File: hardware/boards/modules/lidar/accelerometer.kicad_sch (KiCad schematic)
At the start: 7 parts, among them J8 Conn_01x04_Socket, U2 BNO055, Y2 32.768kHz

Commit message: REFACTO relinked every kicad projects
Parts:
- U2: footprint accelerometer:BNO055_Hand_Soldering_LGA-28_5.2x3.8mm_P0.5mm -> Package_LGA:LGA-28_5.2x3.8mm_P0.5mm
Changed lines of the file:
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@@
 			)
 		)
-		(property "Footprint" "accelerometer:BNO055_Hand_Soldering_LGA-28_5.2x3.8mm_P0.5mm"
+		(property "Footprint" "Package_LGA:LGA-28_5.2x3.8mm_P0.5mm"
 			(at 148.59 133.35 0)
 			(effects

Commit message: updated main points of the lidar module schematic
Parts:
- C7, C8: value 0.1uF -> 100nF
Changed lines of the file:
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@@
 			)
 		)
-		(property "Value" "0.1uF"
+		(property "Value" "100nF"
 			(at 137.414 93.726 90)
 			(effects
@@
 			)
 		)
-		(property "Value" "0.1uF"
+		(property "Value" "100nF"
 			(at 163.068 137.414 0)
 			(effects

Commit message: lidar PCB
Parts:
- removed J8: Conn_01x04_Socket, Connector_PinHeader_2.54mm:PinHeader_1x04_P2.54mm_Vertical, symbol Connector:Conn_01x04_Socket
- added C14: 100nF, Capacitor_SMD:C_0603_1608Metric_Pad1.08x0.95mm_HandSolder, symbol Device:C
- C15: renamed from C7; value 100nF -> 1uF
- U2: footprint Package_LGA:LGA-28_5.2x3.8mm_P0.5mm -> accelerometer:BNO055_Hand_Soldering_LGA-28_5.2x3.8mm_P0.5mm
- renumbered C9 to C11, C10 to C12, C8 to C13
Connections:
- net 3V3: now also C14.1
- net GND: now also C14.2
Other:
- moved on the sheet: C13

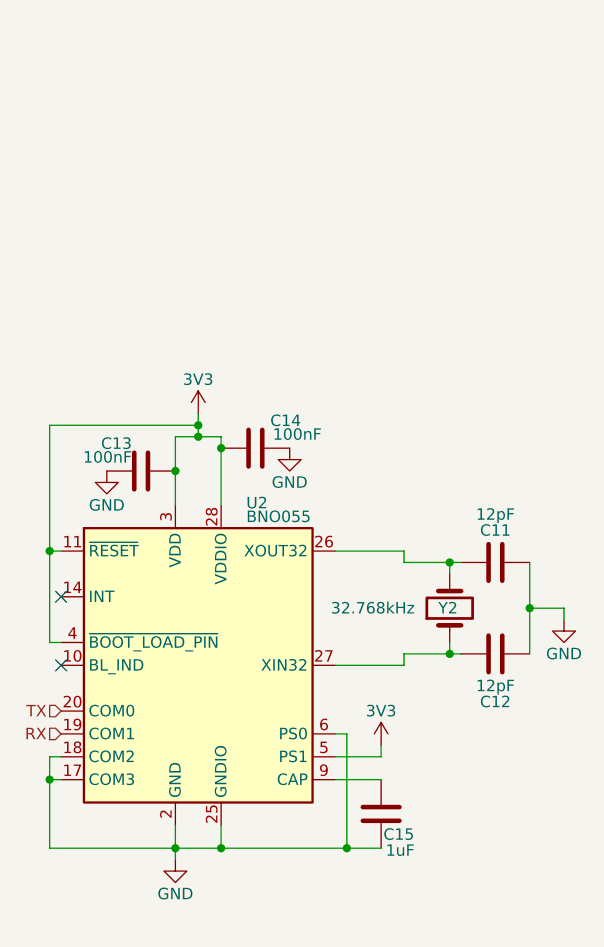
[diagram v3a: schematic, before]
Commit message: change kicad default to custom
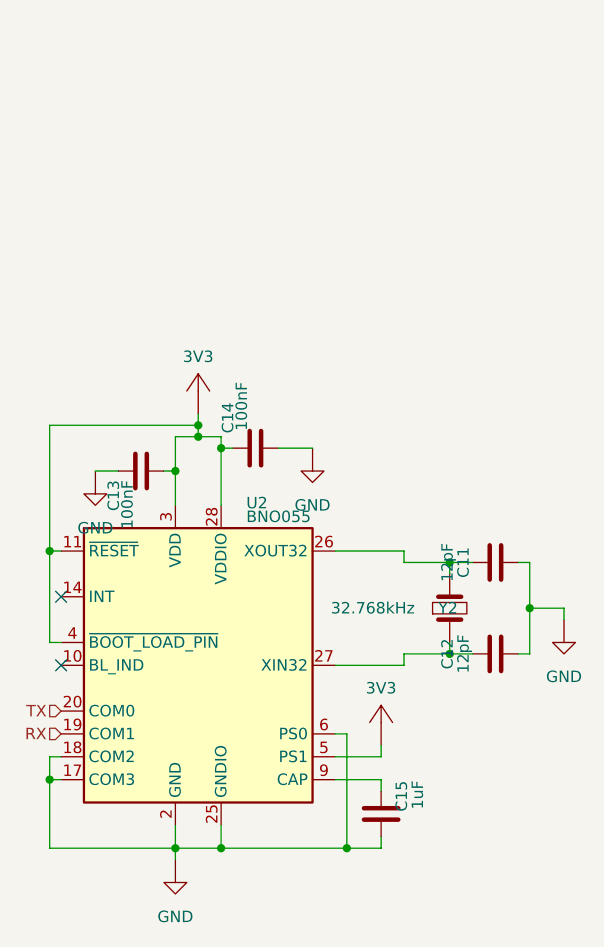
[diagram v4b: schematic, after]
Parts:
- C11, C12, C13, C14, C15: footprint Capacitor_SMD:C_0603_1608Metric_Pad1.08x0.95mm_HandSolder -> common:C_0603; symbol Device:C -> common:Capacitor
- U2: footprint accelerometer:BNO055_Hand_Soldering_LGA-28_5.2x3.8mm_P0.5mm -> Package_LGA:LGA-28_5.2x3.8mm_P0.5mm
- Y2: symbol Device:Crystal -> common:Crystal
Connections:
- net 3V3: now also C13.1, C14.2; no longer C13.2, C14.1
- net GND: now also C12.1, C13.2, C14.1, C15.1; no longer C12.2, C13.1, C14.2, C15.2
- net at U2.27 (XIN32), Y2.1: now also C12.2; no longer C12.1
- net at U2.9 (CAP): now also C15.2; no longer C15.1
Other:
- moved on the sheet: C11, C12, C13, C14, C15
